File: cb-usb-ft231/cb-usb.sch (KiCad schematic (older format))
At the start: 24 parts, among them P1 CONN_01X14, P2 CONN_01X14, P3 CONN_01X05, SW1 SW_PUSH_SMALL, U1 ANTENNA, U2 FT231XS, U3 AP7365-33, U4 LY-SK10

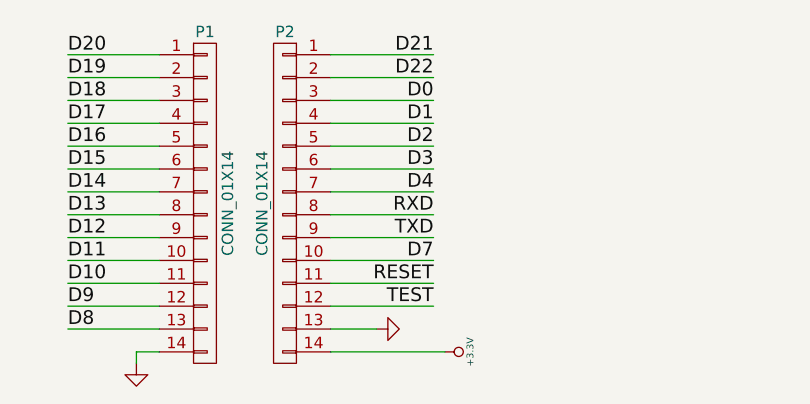
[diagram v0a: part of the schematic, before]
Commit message: RESET and TEST lines forwarded to the right lines
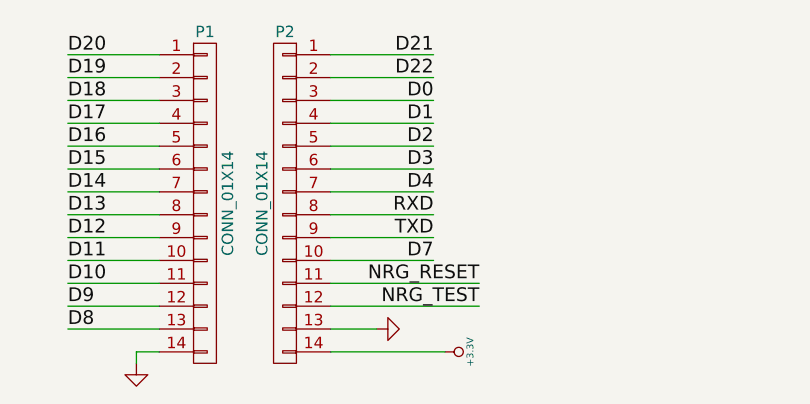
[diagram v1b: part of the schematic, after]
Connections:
- net NRG_RESET: now also P2.11 (P11)
- net NRG_TEST: now also P2.12 (P12)
- net RESET: no longer P2.11 (P11)
- net TEST: no longer P2.12 (P12)
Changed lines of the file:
@@
 $EndComp
 NoConn ~ 6000 3150
-Text Label 3750 7000 2    60   ~ 0
-TEST
-Text Label 3750 6900 2    60   ~ 0
-RESET
+Text Label 3950 7000 2    60   ~ 0
+NRG_TEST
+Text Label 3950 6900 2    60   ~ 0
+NRG_RESET
 Text Label 3750 6800 2    60   ~ 0
 D7
@@
 	3500 7100 3300 7100
 Wire Wire Line
-	3300 6900 3750 6900
-Wire Wire Line
-	3300 7000 3750 7000
+	3300 6900 3950 6900
+Wire Wire Line
+	3300 7000 3950 7000
 Wire Wire Line
 	1650 4850 2450 4850
